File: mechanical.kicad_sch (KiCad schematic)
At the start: 16 parts

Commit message: Additional cleanup
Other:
- title: (none) -> GPU Cluster Backplane
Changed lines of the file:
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@@
   (paper "A3")
   (title_block
+    (title "GPU Cluster Backplane")
+    (date "2023-10-18")
     (rev "1.0.0")
     (comment 1 "www.antmicro.com")

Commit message: Implement changes suggested in schematic review
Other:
- company: (none) -> Antmicro Ltd
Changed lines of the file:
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@@
   (title_block
     (title "GPU Cluster Backplane")
-    (date "2023-10-18")
+    (date "2023-11-09")
     (rev "1.0.0")
+    (company "Antmicro Ltd")
     (comment 1 "www.antmicro.com")
-    (comment 2 "Antmicro Ltd.")
   )
   (wire (pts (xy 128.27 139.7) (xy 128.27 134.62))

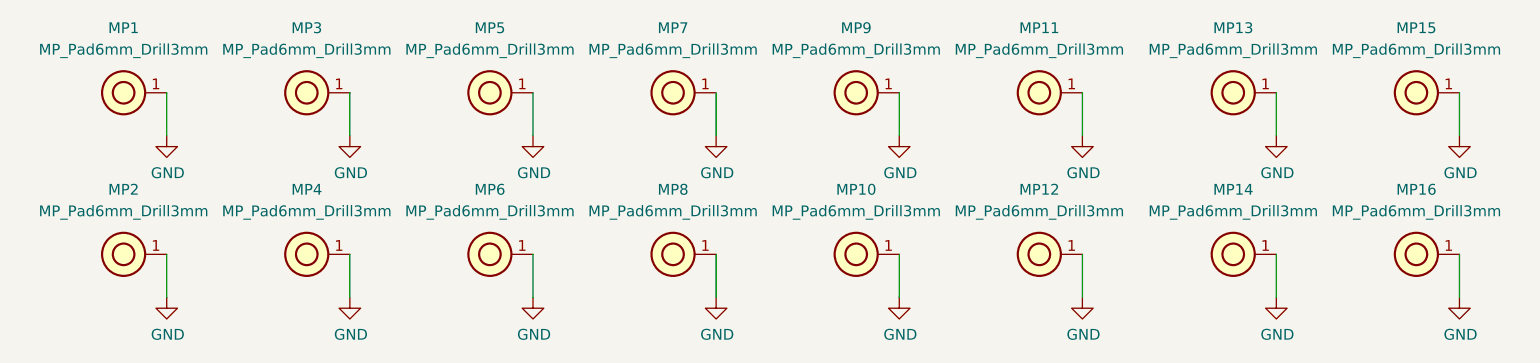
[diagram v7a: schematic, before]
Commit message: Delete unused mechanicals and replace usb symbol
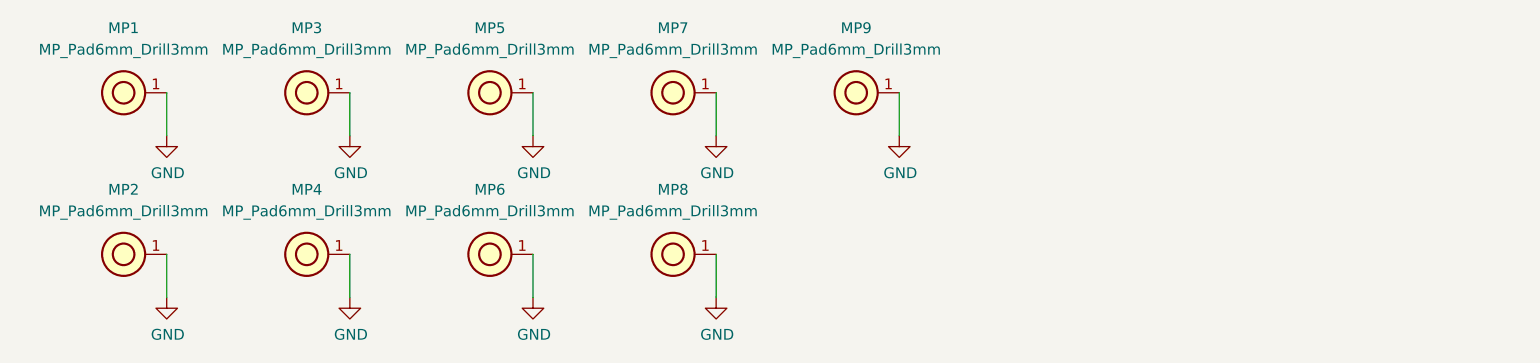
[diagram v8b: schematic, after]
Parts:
- removed MP10, MP11, MP12, MP13, MP14, MP15, MP16: MP_Pad6mm_Drill3mm, antmicro-footprints:MP_Pad6mm_Drill3mm, symbol antmicroMechanicalParts:MP_Pad6mm_Drill3mm
